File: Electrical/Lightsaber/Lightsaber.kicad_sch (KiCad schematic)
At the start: 104 parts, among them J1 USB4105-GF-A, J2 54, J3 54, J4 S2B-XH-A-1, J5 S2B-XH-A-1, J6 S2B-XH-A-1, J7 S3B-XH-A-1, J8 S3B-XH-A-1, Q1 BC817, Q2 BC817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

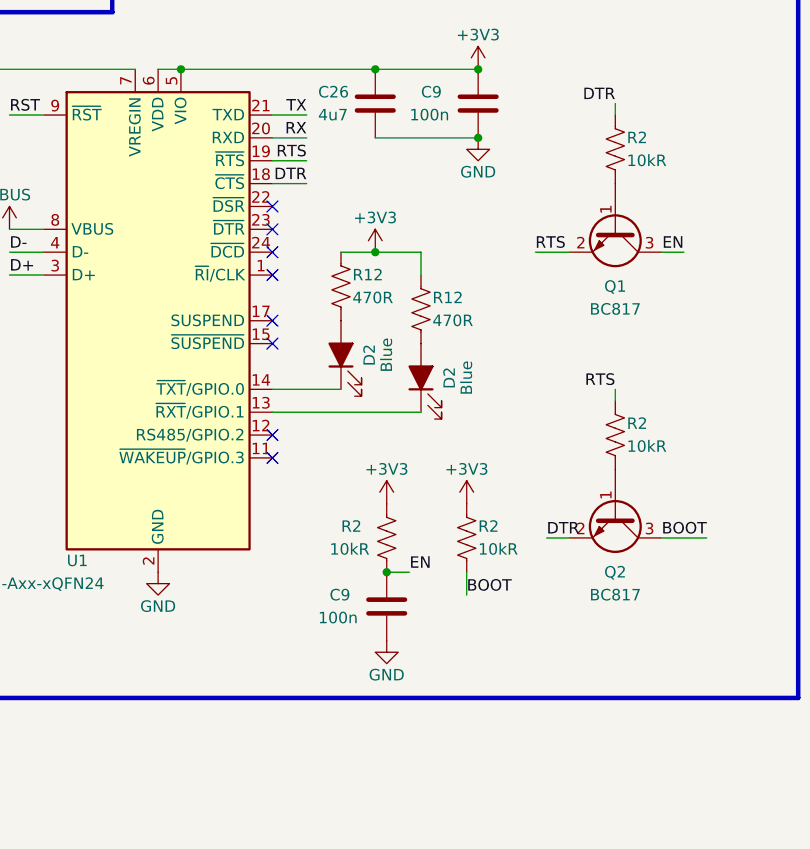
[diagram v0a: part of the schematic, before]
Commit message: made some testing code to test speaker
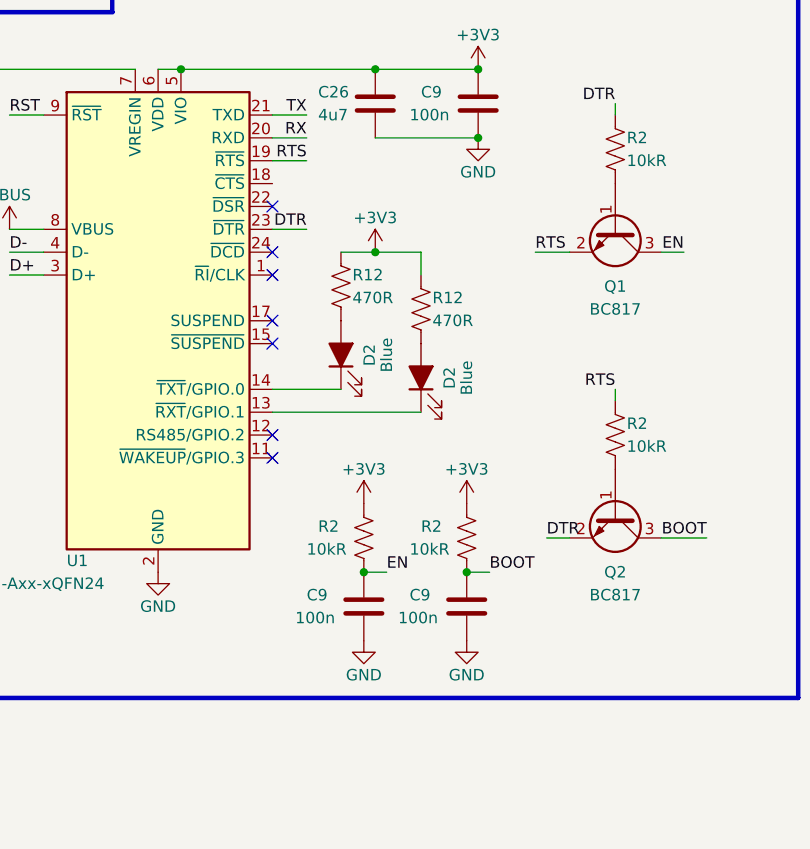
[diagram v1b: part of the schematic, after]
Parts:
- added C9: 100n, Capacitor_SMD:C_0603_1608Metric_Pad1.08x0.95mm_HandSolder, symbol Device:C
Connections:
- net BOOT: now also C9.1
- net DTR: now also U1.23 (~{DTR}); no longer U1.18 (~{CTS})
- net GND: now also C9.2
- no-connect marks 33 -> 32
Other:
- moved on the sheet: C9, R2

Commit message: Switched over to jst ph connectors
wrote test code as well
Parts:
- removed BT1: 18650 battery, Miguel:18650, symbol Miguel:18650
- removed J2, J3: 54, Miguel:54, symbol Connector:Conn_01x01_Pin
- removed J4, J5, J6: S2B-XH-A-1, Miguel:S2B-XH-A-1, symbol Miguel:S2B-XH-A-1
- removed J7, J8: S3B-XH-A-1, Miguel:S3B-XH-A-1, symbol Miguel:S3B-XH-A-1
- added J2, J3, J4, J5: B2B-PH-SM4-TB, Connector_JST:JST_PH_B2B-PH-SM4-TB_1x02-1MP_P2.00mm_Vertical, symbol Miguel:B2B-PH-SM4-TB
- added J6, J7: B3B-PH-SM4-TB, Connector_JST:JST_PH_B3B-PH-SM4-TB_1x03-1MP_P2.00mm_Vertical, symbol Miguel:B3B-PH-SM4-TB
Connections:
- net +3V3: now also J3.1 (Pin_1), J4.1 (Pin_1)
- net +5V: now also J6.1 (Pin_1), J7.1 (Pin_1)
- net +BATT: now also J2.1 (Pin_1)
- net BTN_1: now also J3.2 (Pin_2)
- net BTN_2: now also J4.2 (Pin_2)
- net DOUT_1: now also J6.2 (Pin_2)
- net DOUT_2: now also J7.2 (Pin_2)
- net GND: now also J2.2 (Pin_2), J5.2 (Pin_2), J6.3 (Pin_3), J7.3 (Pin_3)
- net SPKR_OUT: now also J5.1 (Pin_1)
